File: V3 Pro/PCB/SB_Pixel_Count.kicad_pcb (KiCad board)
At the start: 2 copper layers, 53.5 x 26.5 mm, 18 parts, among them J2 String1, J3 OLED, SW1 Test, U1 74AHCT1G125, U2 MOUDLE-SEEEDUINO-XIAO, U3 AMS1117-5.0, U4 INA219BxD

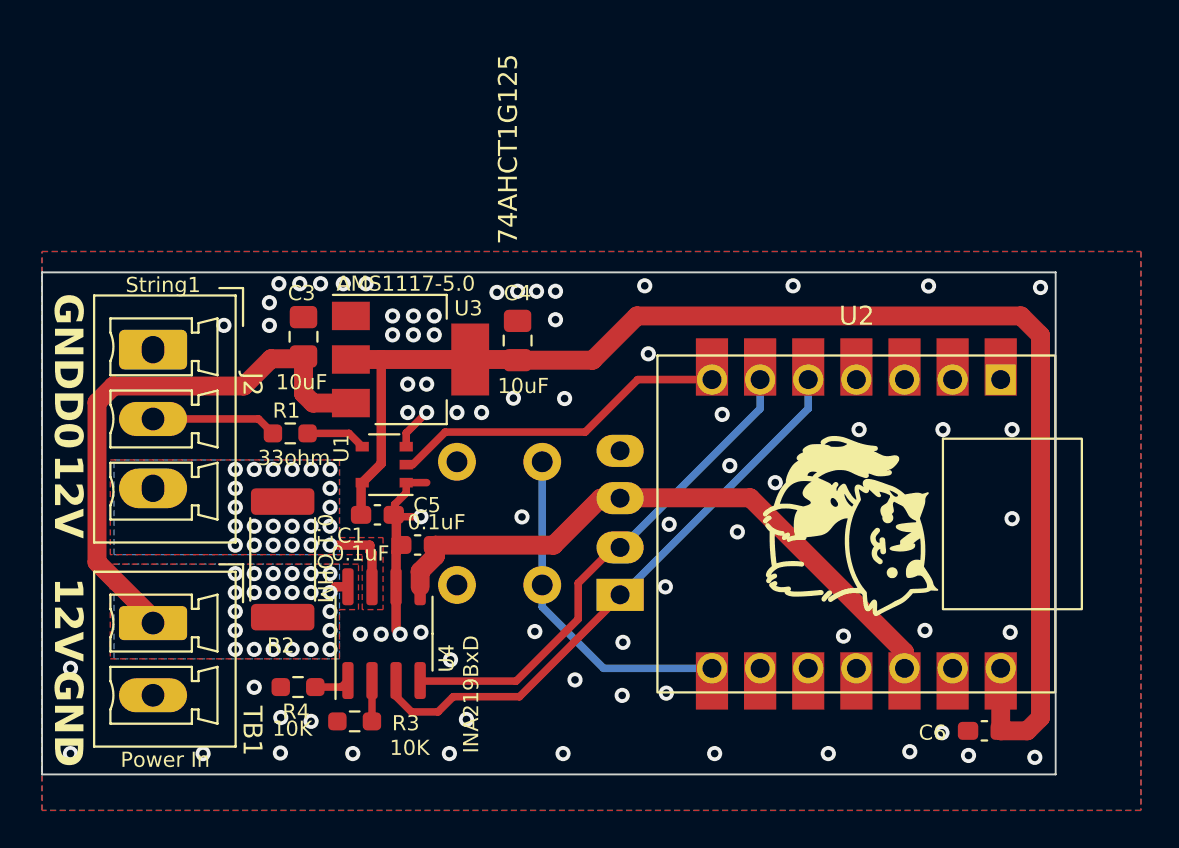
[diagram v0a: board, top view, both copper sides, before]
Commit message: Rename RP2040_Count files/folders to SB_Pixel_Count across all variants
Renames the KiCad project quads (.kicad_pcb/.kicad_sch/.kicad_pro/.kicad_prl),
exported BOM/gerber/production files, case STL/FCStd files, and the
Firmware/RP2040_Count sketch (-> Firmware/SB_Pixel_Count, matching the
required folder/.ino name convention) in V1, V2, V2 Lite, and V3 Pro.

Fixes up internal cross-references that would otherwise go stale:
- kicad_pcb sheetfile metadata and kicad_sch symbol instance "project" fields
- kicad_pro/kicad_prl self-referencing "filename" fields and bom_export_filename
- .github/workflows/compile.yml and drc.yml sketch/DRC paths
- README.md links and ATtiny1614_Count.ino header comments

Verified the renamed Firmware/SB_Pixel_Count sketch still compiles
(VERSION2/seeed_xiao_rp2040) after the rename.

Co-Authored-By: Claude Sonnet 5 <noreply@anthropic.com>
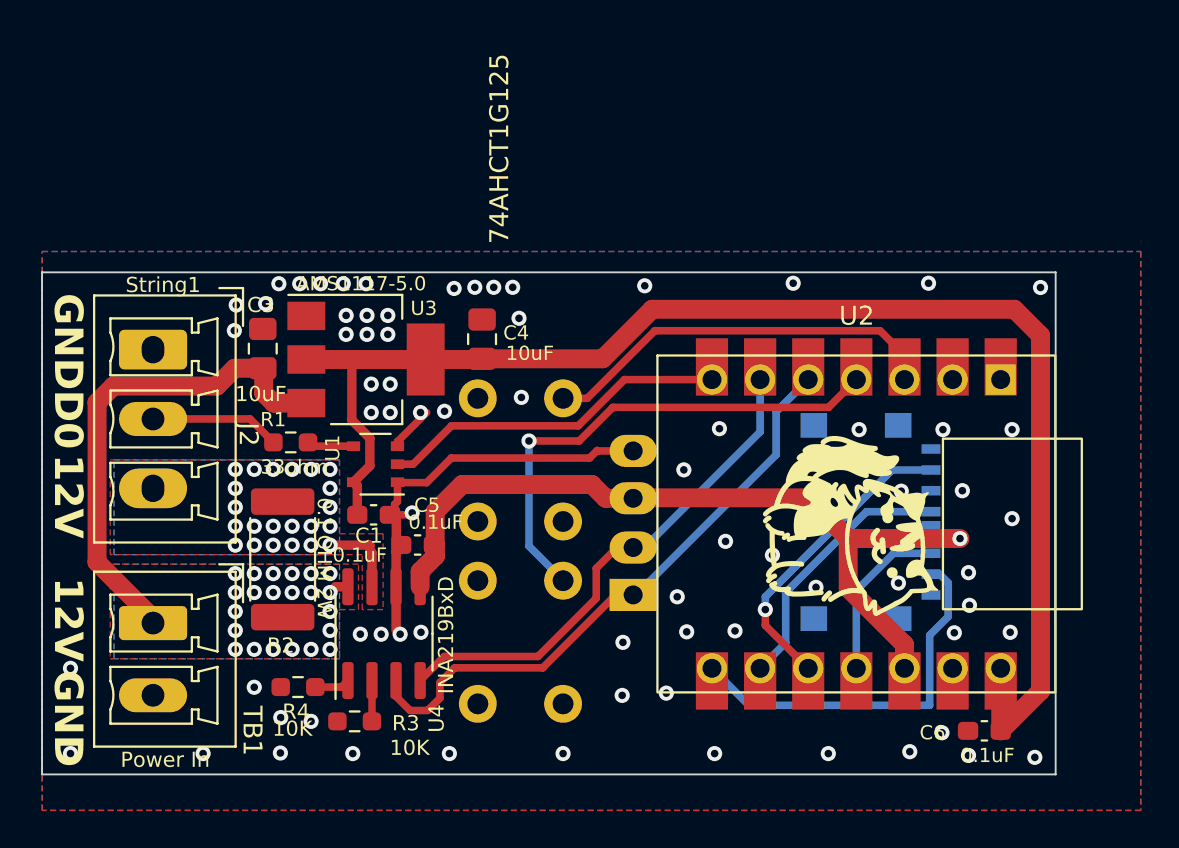
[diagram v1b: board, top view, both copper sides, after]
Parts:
- added SW2: Test, Button_Switch_THT:SW_PUSH_6mm, B.Cu at (127.0, 96.4)
- added U5: TF-123-ARP9H17, TF-SMD_TF:TF-SMD_TF-123-ARP9H15, B.Cu at (143.3, 86.8)
- R2: value 0.1 OHM -> 0.1 OHM 2W
- moved SW1 3.53 mm to (127.0, 86.8)
- moved U3 2.35 mm to (116.6, 78.2)
- moved C3 2.24 mm to (111.2, 77.6)
- moved C4 1.88 mm to (122.7, 77.1)
- moved J3 0.69 mm to (130.7, 86.8)
- moved R1 0.48 mm to (112.6, 82.6)
- moved U1 0.46 mm to (117.1, 83.7)
- moved C1 0.20 mm to (117.0, 86.4)
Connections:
- U2 pad 10: unconnected-(U2-PA5_A9_D9_MISO-Pad10) -> DO
- U2 pad 11: unconnected-(U2-PA6_A10_D10_MOSI-Pad11) -> DI
- U2 pad 3: unconnected-(U2-PA10_A2_D2-Pad3) -> SW1
- U2 pad 4: unconnected-(U2-PA11_A3_D3-Pad4) -> SW2
- U2 pad 8: SW1 -> CS
- U2 pad 9: unconnected-(U2-PA7_A8_D8_SCK-Pad9) -> CLK
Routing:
- net SW2: track 0.00 -> 26.7 mm, vias 0 -> 1
- net CS: track 0.00 -> 20.3 mm
- net DO: track 0.00 -> 16.2 mm, vias 0 -> 1
- net CLK: track 0.00 -> 14.0 mm
- net GND: track 13.5 -> 25.6 mm
- net +3.3V: track 32.6 -> 43.4 mm, vias 0 -> 1
- net DI: track 0.00 -> 8.86 mm
- net SW1: track 18.0 -> 21.6 mm
- net VIN1: track 30.5 -> 27.7 mm
- net +5V: track 72.3 -> 74.1 mm
- net I2C_SDA: track 31.1 -> 32.0 mm
- net Net-(R1-Pad2): track 3.18 -> 2.49 mm
- net I2C_SCL: track 26.6 -> 27.1 mm
